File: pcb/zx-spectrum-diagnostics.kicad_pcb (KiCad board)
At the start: 2 copper layers, 99.9 x 79.9 mm, 88 parts, among them J101 Conn_01x04, J102 Conn_01x03_Male, J103 Conn_01x03_Male, J201 Conn_01x20_Female, J202 Conn_01x20_Female, J203 Conn_01x20_Female, J204 Conn_01x20_Female, J205 Conn_01x20_Female, Q101 PMBT2222A, SW101 SW_SPST, SW102 SW_SPST, U101 Pico, U102 Pico

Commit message: schematic reworked, it's time to relayout the board. checkpoint here
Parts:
- removed J204: Conn_01x20_Female, Connector_PinSocket_2.54mm:PinSocket_1x20_P2.54mm_Vertical
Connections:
- J201 pad 18: ZXMIN5V -> ZXWAIT
- J201 pad 19: ZXWAIT -> ZXM1
- J201 pad 20: ZX12V -> ZXRFSH
- J202 pad 1: ZXROMCS -> ZXA8
- J202 pad 13: unconnected-(J202-Pad13) -> P1_BLIPPER
- J202 pad 14: unconnected-(J202-Pad14) -> P2_BLIPPER
- J202 pad 15: unconnected-(J202-Pad15) -> P2_GPIO26
- J202 pad 16: unconnected-(J202-Pad16) -> P2_GPIO27
- J202 pad 17: unconnected-(J202-Pad17) -> P2_GPIO28
- J202 pad 18: unconnected-(J202-Pad18) -> ZX9V
- J202 pad 19: unconnected-(J202-Pad19) -> ZXMIN5V
- J202 pad 2: ZXBUSACK -> ZXA10
- J202 pad 20: unconnected-(J202-Pad20) -> ZX12V
- J202 pad 3: ZXA9 -> ZXA11
- J202 pad 4: ZXA11 -> ZXA9
- J202 pad 5: ZX12VAC -> ZXBUSACK
- J202 pad 6: ZXM1 -> PICO_SIGNAL
- J202 pad 7: ZXRFSH -> P2_GPIO16
- J202 pad 8: ZXA8 -> P2_GPIO17
- J202 pad 9: ZXA10 -> P2_GPIO18
- J203 pad 10: ZXIORQGE -> ZXVIDEO
- J203 pad 11: ZXVIDEO -> ZXY
- J203 pad 12: ZXY -> ZXV
- J203 pad 13: ZXV -> ZXU
- J203 pad 14: ZXU -> ZXBUSRQ
- J203 pad 15: ZXBUSRQ -> ZXRESET
- J203 pad 16: ZXRESET -> ZXA7
- J203 pad 17: ZXA7 -> ZXA6
- J203 pad 18: ZXA6 -> ZXA5
- J203 pad 19: ZXA5 -> ZXA4
- J203 pad 20: ZXA4 -> ZXROMCS
- J203 pad 4: ZX9V -> ZXCLK
- J203 pad 5: ZXCLK -> ZXA0
- J203 pad 6: ZXA0 -> ZXA1
- J203 pad 7: ZXA1 -> ZXA2
- J203 pad 8: ZXA2 -> ZXA3
- J203 pad 9: ZXA3 -> ZXIORQGE
- J205 pad 1: P2_GPIO4 -> ZXA4
- J205 pad 10: P2_GPIO13 -> ZXA13
- J205 pad 11: P2_GPIO14 -> ZXA14
- J205 pad 12: P2_GPIO15 -> ZXA15
- J205 pad 2: P2_GPIO5 -> ZXA5
- J205 pad 3: P2_GPIO6 -> ZXA6
- J205 pad 4: P2_GPIO7 -> ZXA7
- J205 pad 5: P2_GPIO8 -> ZXA8
- J205 pad 6: P2_GPIO9 -> ZXA9
- J205 pad 7: P2_GPIO10 -> ZXA10
- J205 pad 8: P2_GPIO11 -> ZXA11
- J205 pad 9: P2_GPIO12 -> ZXA12
- U101 pad 1: P1_GPIO0 -> ZXD0
- U101 pad 10: P1_GPIO7 -> ZXD7
- U101 pad 11: P1_GPIO8 -> PICO_SIGNAL
- U101 pad 12: P1_GPIO9 -> P1_BLIPPER
- U101 pad 14: P1_GPIO10 -> ZXMREQ
- U101 pad 15: P1_GPIO11 -> ZXRD
- U101 pad 16: P1_GPIO12 -> ZXWR
- U101 pad 17: P1_GPIO13 -> ZXM1
- U101 pad 19: P1_GPIO14 -> ZXCLK
- U101 pad 2: P1_GPIO1 -> ZXD1
- U101 pad 20: P1_GPIO15 -> ZXINT
- U101 pad 4: P1_GPIO2 -> ZXD2
- U101 pad 5: P1_GPIO3 -> ZXD3
- U101 pad 6: P1_GPIO4 -> ZXD4
- U101 pad 7: P1_GPIO5 -> ZXD5
- U101 pad 9: P1_GPIO6 -> ZXD6
- U102 pad 1: P2_GPIO0 -> ZXA0
- U102 pad 10: P2_GPIO7 -> ZXA7
- U102 pad 11: P2_GPIO8 -> ZXA8
- U102 pad 12: P2_GPIO9 -> ZXA9
- U102 pad 14: P2_GPIO10 -> ZXA10
- U102 pad 15: P2_GPIO11 -> ZXA11
- U102 pad 16: P2_GPIO12 -> ZXA12
- U102 pad 17: P2_GPIO13 -> ZXA13
- U102 pad 19: P2_GPIO14 -> ZXA14
- U102 pad 2: P2_GPIO1 -> ZXA1
- U102 pad 20: P2_GPIO15 -> ZXA15
- U102 pad 25: P2_GPIO19 -> P2_BLIPPER
- U102 pad 26: P2_GPIO20 -> PICO_SIGNAL
- U102 pad 4: P2_GPIO2 -> ZXA2
- U102 pad 5: P2_GPIO3 -> ZXA3
- U102 pad 6: P2_GPIO4 -> ZXA4
- U102 pad 7: P2_GPIO5 -> ZXA5
- U102 pad 9: P2_GPIO6 -> ZXA6
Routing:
- net P2_GPIO3: track 124.9 -> 0.00 mm, vias 3 -> 0
- net P2_GPIO2: track 116.3 -> 0.00 mm, vias 3 -> 0
- net P2_GPIO1: track 104.3 -> 0.00 mm, vias 2 -> 0
- net P2_GPIO0: track 94.8 -> 0.00 mm, vias 2 -> 0
- net ZXA9: track 27.9 -> 98.7 mm, vias 3 -> 6
- net PICO_SIGNAL: track 0.00 -> 57.6 mm, vias 0 -> 2
- net ZXA10: track 38.1 -> 91.8 mm, vias 3 -> 8
- net P2_GPIO9: track 38.2 -> 0.00 mm, vias 2 -> 0
- net ZXA15: track 12.3 -> 50.0 mm, vias 0 -> 2
- net P2_GPIO15: track 37.7 -> 0.00 mm, vias 2 -> 0
- net P2_GPIO8: track 36.6 -> 0.00 mm, vias 2 -> 0
- net ZXA14: track 10.7 -> 46.8 mm, vias 0 -> 2
- net P2_GPIO14: track 36.2 -> 0.00 mm, vias 2 -> 0
- net P2_GPIO7: track 34.6 -> 0.00 mm, vias 2 -> 0
- net ZXA7: track 16.9 -> 51.5 mm, vias 0 -> 2
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
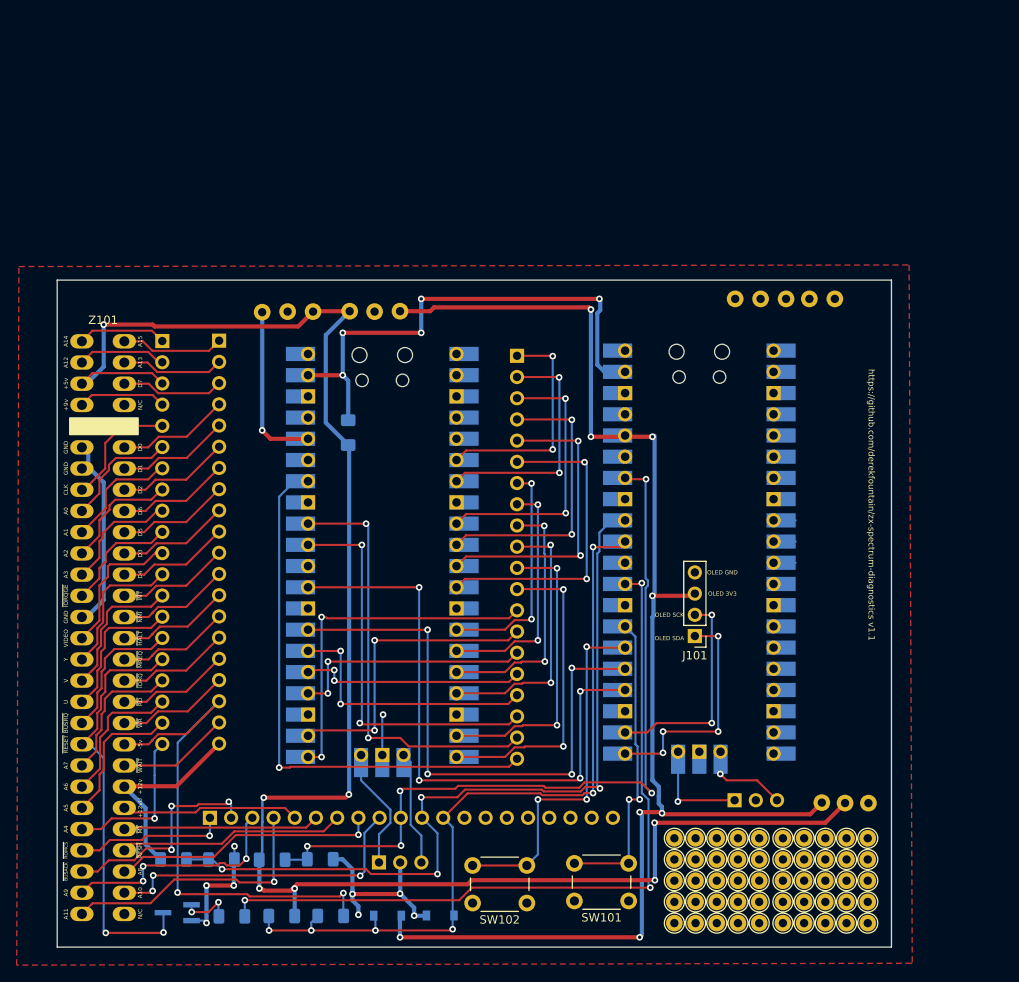
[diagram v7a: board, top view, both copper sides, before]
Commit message: sorted out the pico orientation and the edge connector connections
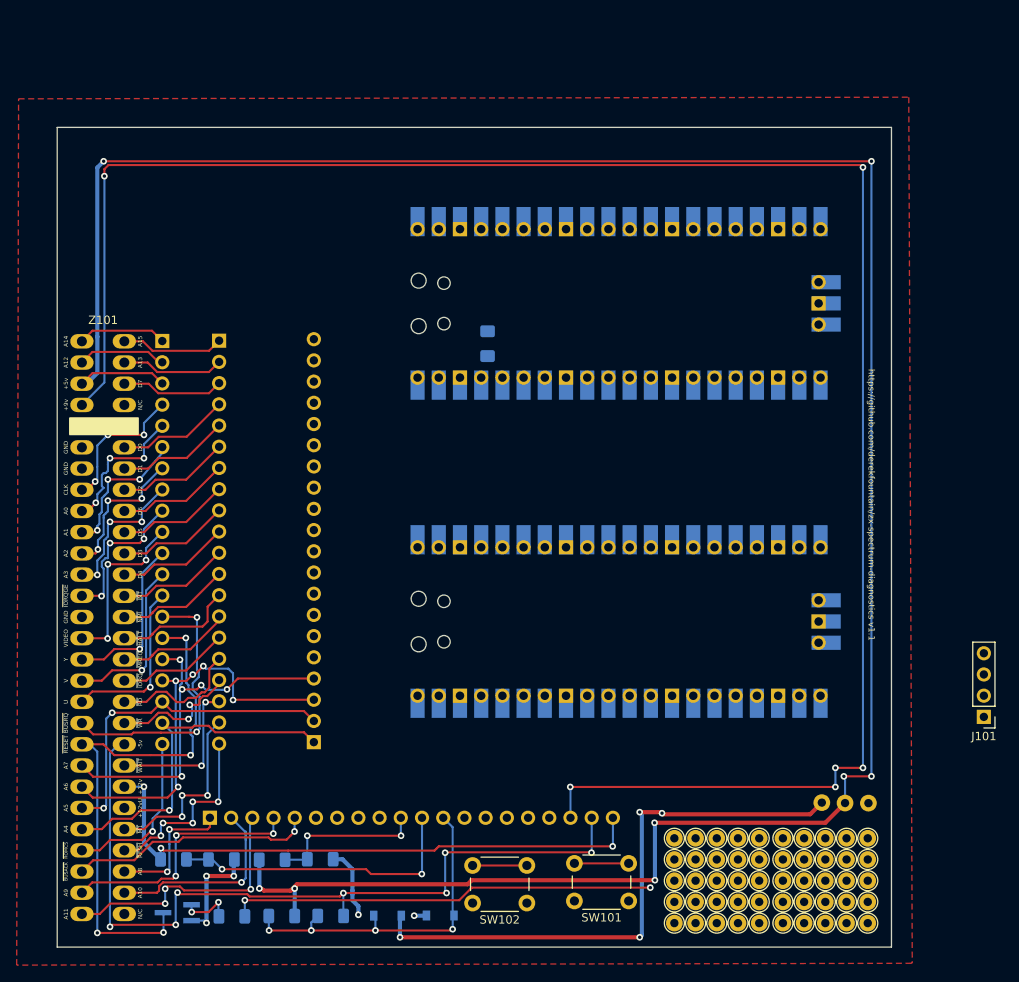
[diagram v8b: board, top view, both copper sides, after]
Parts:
- removed the ? at (158.9, 76.4)
- removed the ? at (112.7, 77.9)
- removed the ? at (105.3, 77.9)
- removed the ? at (167.8, 76.4)
- removed the ? at (155.9, 76.4)
- removed the ? at (109.7, 77.9)
- removed the ? at (99.2, 78.0)
- removed the ? at (102.3, 77.9)
- removed the ? at (162.0, 76.4)
- removed the ? at (115.8, 77.9)
- removed the ? at (164.8, 76.4)
- removed J102, J103: Conn_01x03_Male, Connector_PinSocket_2.54mm:PinSocket_1x03_P2.54mm_Vertical
- moved J205 52.3 mm to (105.4, 129.5), turned to 0 degrees
- moved U102 41.4 mm to (142.0, 77.0), turned to -90 degrees
- moved J101 35.9 mm to (185.7, 126.5)
- moved D101 19.8 mm to (126.2, 81.8), turned to 90 degrees
- moved U101 12.7 mm to (142.0, 115.1), turned to -90 degrees
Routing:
- net ZX9V: track 10.6 -> 233.5 mm, vias 0 -> 6
- net 3V3_PICO1: track 164.7 -> 68.8 mm, vias 8 -> 4
- net +5V: track 211.4 -> 295.3 mm, vias 7 -> 8
- net 5V_DIV: track 93.8 -> 18.8 mm, vias 5 -> 2
- net P2_LINKOUT: track 71.7 -> 0.00 mm, vias 4 -> 0
- net P2_GPIO16: track 69.1 -> 0.00 mm, vias 2 -> 0
- net ZXA9: track 98.7 -> 30.6 mm, vias 6 -> 3
- net P2_LINKIN: track 68.0 -> 0.00 mm, vias 4 -> 0
- net P2_GPIO17: track 67.9 -> 0.00 mm, vias 3 -> 0
- net ZXA10: track 91.8 -> 24.5 mm, vias 8 -> 1
- net P2_GPIO28: track 64.0 -> 0.00 mm, vias 1 -> 0
- net 12V_DIV: track 95.4 -> 35.2 mm, vias 4 -> 2
- net PICO_PWR: track 59.8 -> 0.00 mm, vias 5 -> 0
- net PICO_SIGNAL: track 57.6 -> 0.00 mm, vias 2 -> 0
- net MIN5V_DIV: track 94.3 -> 41.4 mm, vias 6 -> 4
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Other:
- board size 99.9 x 79.9 mm -> 99.9 x 98.2 mm
- board text removed: "OLED 3V3"
- board text removed: "OLED GND"
- board text removed: "OLED SCK"
- board text removed: "OLED SDA"
- board text removed: "P1-0"
- board text removed: "P1-1"
- board text removed: "P1-10"
- board text removed: "P1-11"
- board text removed: "P1-12"
- board text removed: "P1-13"
- board text removed: "P1-14"
- board text removed: "P1-15"
- board text removed: "P1-2"
- board text removed: "P1-3"
- board text removed: "P1-4"
- board text removed: "P1-5"
- board text removed: "P1-6"
- board text removed: "P1-7"
- board text removed: "P1-8"
- board text removed: "P1-9"
- board text removed: "P2-0"
- board text removed: "P2-1"
- board text removed: "P2-10"
- board text removed: "P2-11"
- board text removed: "P2-12"
- board text removed: "P2-13"
- board text removed: "P2-14"
- board text removed: "P2-15"
- board text removed: "P2-16"
- board text removed: "P2-17"
- board text removed: "P2-18"
- board text removed: "P2-19"
- board text removed: "P2-2"
- board text removed: "P2-20"
- board text removed: "P2-26"
- board text removed: "P2-27"
- board text removed: "P2-28"
- board text removed: "P2-3"
- board text removed: "P2-4"
- board text removed: "P2-5"
- board text removed: "P2-6"
- board text removed: "P2-7"
- board text removed: "P2-8"
- board text removed: "P2-9"
